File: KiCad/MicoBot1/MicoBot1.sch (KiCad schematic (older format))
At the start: 20 parts, among them J1 Prog, J2 Bat, J3 Motor2, J4 Motor1, J5 Datos, J6 Vcc, J7 Gnd, SW1 Rst, SW2 On, U1 ATmega328P-PU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

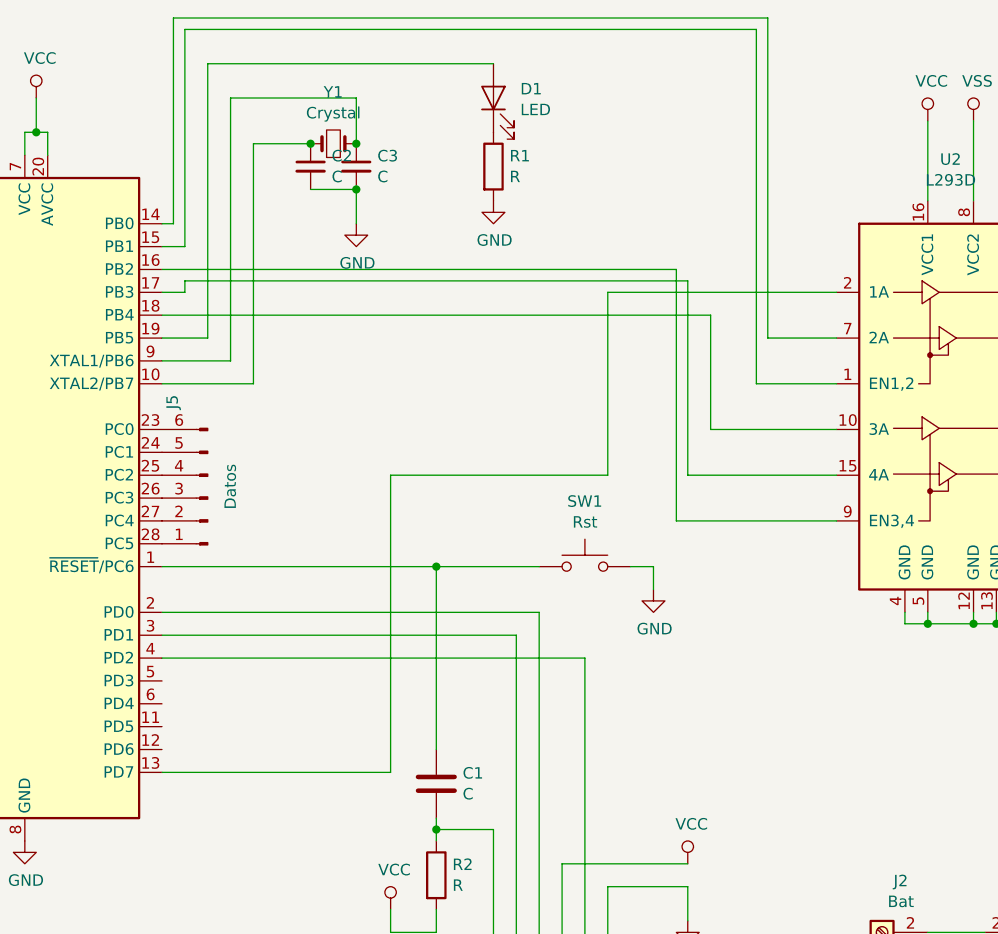
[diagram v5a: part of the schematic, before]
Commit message: 
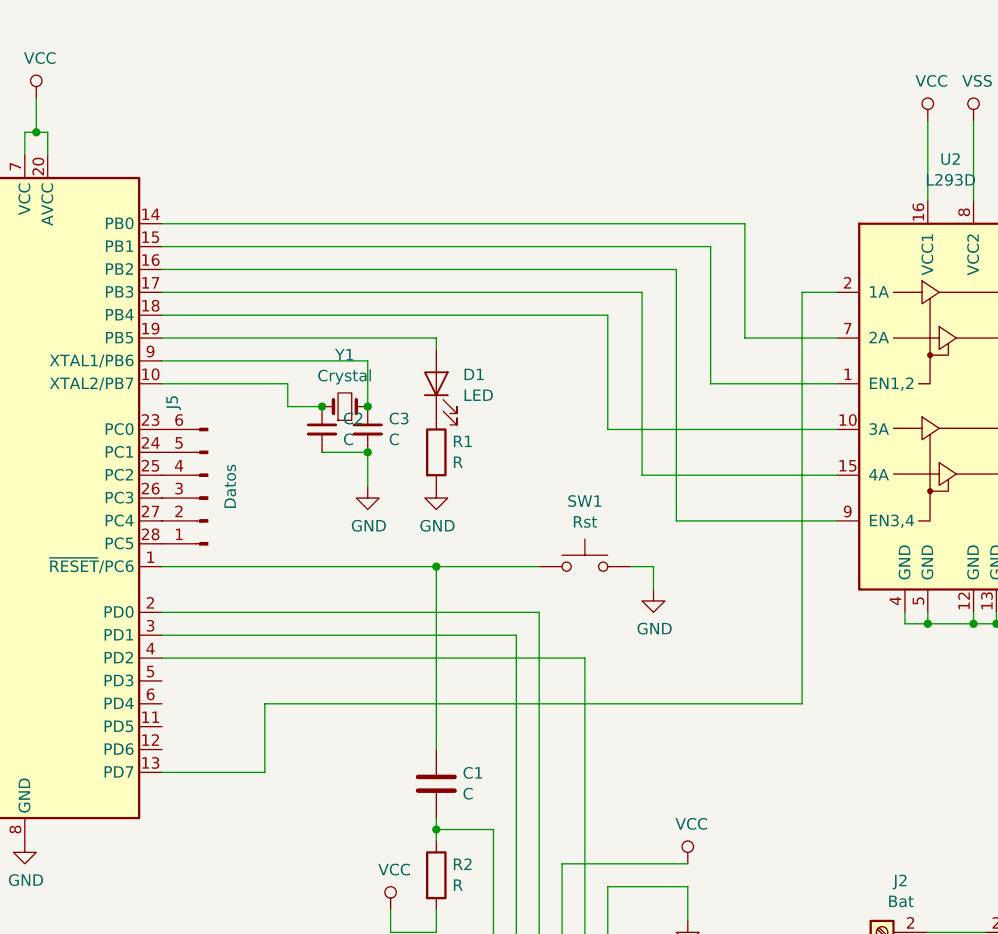
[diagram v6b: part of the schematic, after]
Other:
- moved on the sheet: C2, C3, D1, R1, Y1
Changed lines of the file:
@@
 L Device:LED D1
 U 1 1 5CB896AF
-P 5600 1200
-F 0 "D1" V 5639 1083 50  0000 R CNN
-F 1 "LED" V 5548 1083 50  0000 R CNN
-F 2 "LED_THT:LED_D3.0mm" H 5600 1200 50  0001 C CNN
-F 3 "~" H 5600 1200 50  0001 C CNN
-	1    5600 1200
+P 5350 2450
+F 0 "D1" V 5389 2333 50  0000 R CNN
+F 1 "LED" V 5298 2333 50  0000 R CNN
+F 2 "LED_THT:LED_D3.0mm" H 5350 2450 50  0001 C CNN
+F 3 "~" H 5350 2450 50  0001 C CNN
+	1    5350 2450
 	0    -1   -1   0
 $EndComp
@@
 L Device:R R1
 U 1 1 5CB8BF62
-P 5600 1500
-F 0 "R1" H 5670 1546 50  0000 L CNN
-F 1 "R" H 5670 1455 50  0000 L CNN
-F 2 "Resistor_THT:R_Axial_DIN0204_L3.6mm_D1.6mm_P5.08mm_Horizontal" V 5530 1500 50  0001 C CNN
-F 3 "~" H 5600 1500 50  0001 C CNN
-	1    5600 1500
+P 5350 2750
+F 0 "R1" H 5420 2796 50  0000 L CNN
+F 1 "R" H 5420 2705 50  0000 L CNN
+F 2 "Resistor_THT:R_Axial_DIN0204_L3.6mm_D1.6mm_P5.08mm_Horizontal" V 5280 2750 50  0001 C CNN
+F 3 "~" H 5350 2750 50  0001 C CNN
+	1    5350 2750
 	1    0    0    -1
 $EndComp
@@
 L power:GND #PWR06
 U 1 1 5CB8C74D
-P 5600 1650
-F 0 "#PWR06" H 5600 1400 50  0001 C CNN
-F 1 "GND" H 5605 1477 50  0000 C CNN
-F 2 "" H 5600 1650 50  0001 C CNN
-F 3 "" H 5600 1650 50  0001 C CNN
-	1    5600 1650
+P 5350 2900
+F 0 "#PWR06" H 5350 2650 50  0001 C CNN
+F 1 "GND" H 5355 2727 50  0000 C CNN
+F 2 "" H 5350 2900 50  0001 C CNN
+F 3 "" H 5350 2900 50  0001 C CNN
+	1    5350 2900
 	1    0    0    -1
 $EndComp
@@
 L Device:Crystal_Small Y1
 U 1 1 5CB975FD
-P 4900 1400
-F 0 "Y1" H 4900 1625 50  0000 C CNN
-F 1 "Crystal" H 4900 1534 50  0000 C CNN
-F 2 "Crystal:Crystal_HC49-4H_Vertical" H 4900 1400 50  0001 C CNN
-F 3 "~" H 4900 1400 50  0001 C CNN
-	1    4900 1400
+P 4950 2550
+F 0 "Y1" H 4950 2775 50  0000 C CNN
+F 1 "Crystal" H 4950 2684 50  0000 C CNN
+F 2 "Crystal:Crystal_HC49-4H_Vertical" H 4950 2550 50  0001 C CNN
+F 3 "~" H 4950 2550 50  0001 C CNN
+	1    4950 2550
 	1    0    0    -1
 $EndComp
@@
 L Device:C_Small C2
 U 1 1 5CB99E74
-P 4800 1500
-F 0 "C2" H 4892 1546 50  0000 L CNN
-F 1 "C" H 4892 1455 50  0000 L CNN
-F 2 "Capacitor_THT:C_Disc_D4.3mm_W1.9mm_P5.00mm" H 4800 1500 50  0001 C CNN
-F 3 "~" H 4800 1500 50  0001 C CNN
-	1    4800 1500
+P 4850 2650
+F 0 "C2" H 4942 2696 50  0000 L CNN
+F 1 "C" H 4942 2605 50  0000 L CNN
+F 2 "Capacitor_THT:C_Disc_D4.3mm_W1.9mm_P5.00mm" H 4850 2650 50  0001 C CNN
+F 3 "~" H 4850 2650 50  0001 C CNN
+	1    4850 2650
 	1    0    0    -1
 $EndComp
@@
 L Device:C_Small C3
 U 1 1 5CB9B3E9
-P 5000 1500
-F 0 "C3" H 5092 1546 50  0000 L CNN
-F 1 "C" H 5092 1455 50  0000 L CNN
-F 2 "Capacitor_THT:C_Disc_D4.3mm_W1.9mm_P5.00mm" H 5000 1500 50  0001 C CNN
-F 3 "~" H 5000 1500 50  0001 C CNN
-	1    5000 1500
+P 5050 2650
+F 0 "C3" H 5142 2696 50  0000 L CNN
+F 1 "C" H 5142 2605 50  0000 L CNN
+F 2 "Capacitor_THT:C_Disc_D4.3mm_W1.9mm_P5.00mm" H 5050 2650 50  0001 C CNN
+F 3 "~" H 5050 2650 50  0001 C CNN
+	1    5050 2650
 	1    0    0    -1
 $EndComp
@@
 L power:GND #PWR07
 U 1 1 5CB9B8B0
-P 5000 1750
-F 0 "#PWR07" H 5000 1500 50  0001 C CNN
-F 1 "GND" H 5005 1577 50  0000 C CNN
-F 2 "" H 5000 1750 50  0001 C CNN
-F 3 "" H 5000 1750 50  0001 C CNN
-	1    5000 1750
-	1    0    0    -1
-$EndComp
-Wire Wire Line
-	4800 1600 5000 1600
-Wire Wire Line
-	5000 1750 5000 1600
-Connection ~ 5000 1600
+P 5050 2900
+F 0 "#PWR07" H 5050 2650 50  0001 C CNN
+F 1 "GND" H 5055 2727 50  0000 C CNN
+F 2 "" H 5050 2900 50  0001 C CNN
+F 3 "" H 5050 2900 50  0001 C CNN
+	1    5050 2900
+	1    0    0    -1
+$EndComp
+Wire Wire Line
+	4850 2750 5050 2750
+Wire Wire Line
+	5050 2900 5050 2750
+Connection ~ 5050 2750
 $Comp
 L power:GND #PWR08
@@
 $EndComp
 Wire Wire Line
-	4150 2250 4350 2250
-Wire Wire Line
-	4350 1050 5600 1050
-Wire Wire Line
-	4150 2350 4450 2350
-Wire Wire Line
-	4450 1200 5000 1200
-Wire Wire Line
-	5000 1200 5000 1400
-Connection ~ 5000 1400
-Wire Wire Line
-	4550 1400 4800 1400
-Wire Wire Line
-	4150 2450 4550 2450
-Connection ~ 4800 1400
+	5050 2350 5050 2550
+Connection ~ 5050 2550
+Connection ~ 4850 2550
 $Comp
 L Connector:Screw_Terminal_01x02 J3
@@
 	8250 4950 8300 4950
 Wire Wire Line
-	4150 4150 5150 4150
-Wire Wire Line
-	5150 2850 6100 2850
-Wire Wire Line
-	4150 1750 4200 1750
-Wire Wire Line
-	4200 1750 4200 850
-Wire Wire Line
-	4200 850  6800 850
-Wire Wire Line
-	6800 850  6800 2250
-Wire Wire Line
-	6800 2250 7100 2250
-Wire Wire Line
-	4150 1850 4250 1850
-Wire Wire Line
-	4250 1850 4250 900
-Wire Wire Line
-	4250 900  6750 900
-Wire Wire Line
-	6750 900  6750 2450
-Wire Wire Line
-	6750 2450 7100 2450
-Wire Wire Line
-	6550 2650 7100 2650
-Wire Wire Line
-	6450 2850 7100 2850
-Wire Wire Line
 	6400 3050 7100 3050
-Wire Wire Line
-	6100 2050 6100 2850
-Wire Wire Line
-	5150 2850 5150 4150
-Wire Wire Line
-	4550 1400 4550 2450
-Wire Wire Line
-	4450 1200 4450 2350
-Wire Wire Line
-	4350 1050 4350 2250
-Wire Wire Line
-	6100 2050 7100 2050
-Wire Wire Line
-	6450 2000 4250 2000
-Wire Wire Line
-	4250 2000 4250 2050
-Wire Wire Line
-	4250 2050 4150 2050
-Wire Wire Line
-	6450 2000 6450 2850
 Wire Wire Line
 	4150 1950 6400 1950
@@
 	5350 4850 5350 4750
 Wire Wire Line
-	4150 2150 6550 2150
-Wire Wire Line
-	6550 2150 6550 2650
-Wire Wire Line
 	8600 5250 8600 5350
 $Comp
@@
 Wire Wire Line
 	6000 3650 6000 4950
+Wire Wire Line
+	4150 4150 4600 4150
+Wire Wire Line
+	4600 4150 4600 3850
+Wire Wire Line
+	4600 3850 6950 3850
+Wire Wire Line
+	6950 3850 6950 2050
+Wire Wire Line
+	6950 2050 7100 2050
+Wire Wire Line
+	4150 2150 6100 2150
+Wire Wire Line
+	4150 2050 6250 2050
+Wire Wire Line
+	4700 2550 4850 2550
+Wire Wire Line
+	4150 2350 5050 2350
+Wire Wire Line
+	4700 2450 4700 2550
+Wire Wire Line
+	4150 2450 4700 2450
+Wire Wire Line
+	5350 2300 5350 2250
+Wire Wire Line
+	4150 2250 5350 2250
+Wire Wire Line
+	6100 2650 6100 2150
+Wire Wire Line
+	6100 2650 7100 2650
+Wire Wire Line
+	6250 2850 6250 2050
+Wire Wire Line
+	6250 2850 7100 2850
+Wire Wire Line
+	6550 1850 6550 2450
+Wire Wire Line
+	4150 1850 6550 1850
+Wire Wire Line
+	6550 2450 7100 2450
+Wire Wire Line
+	6700 1750 6700 2250
+Wire Wire Line
+	4150 1750 6700 1750
+Wire Wire Line
+	6700 2250 7100 2250
 $EndSCHEMATC

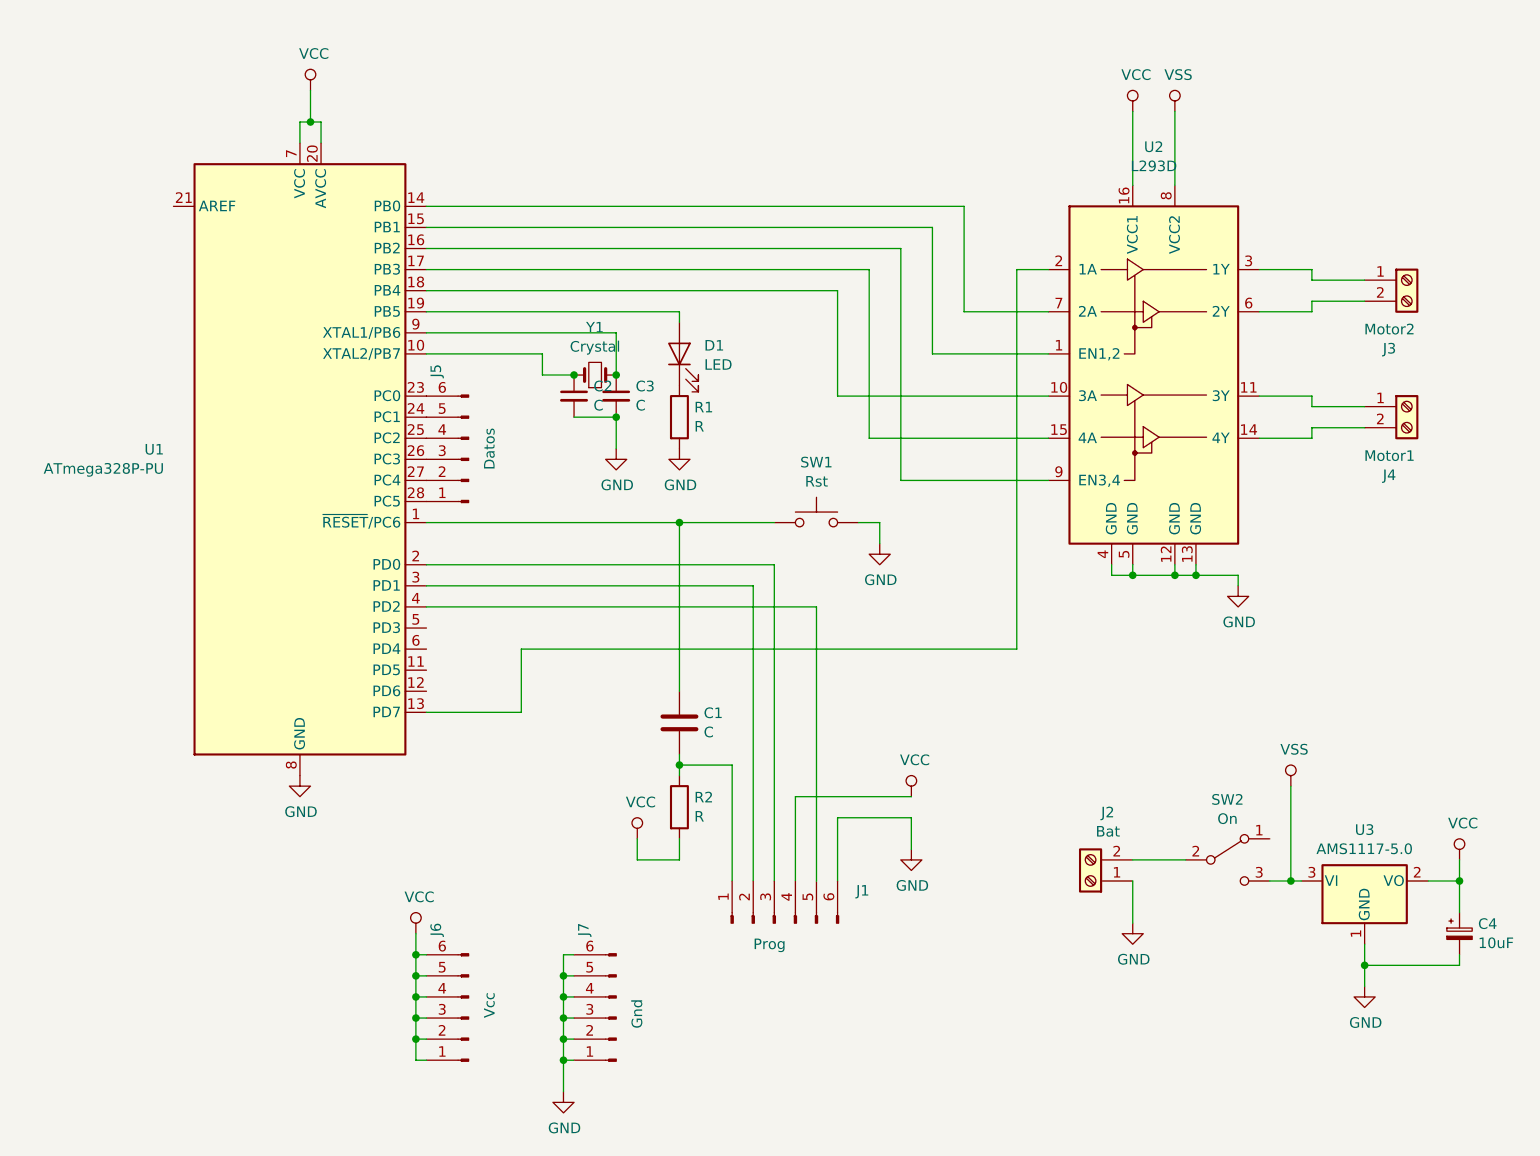
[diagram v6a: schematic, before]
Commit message: 
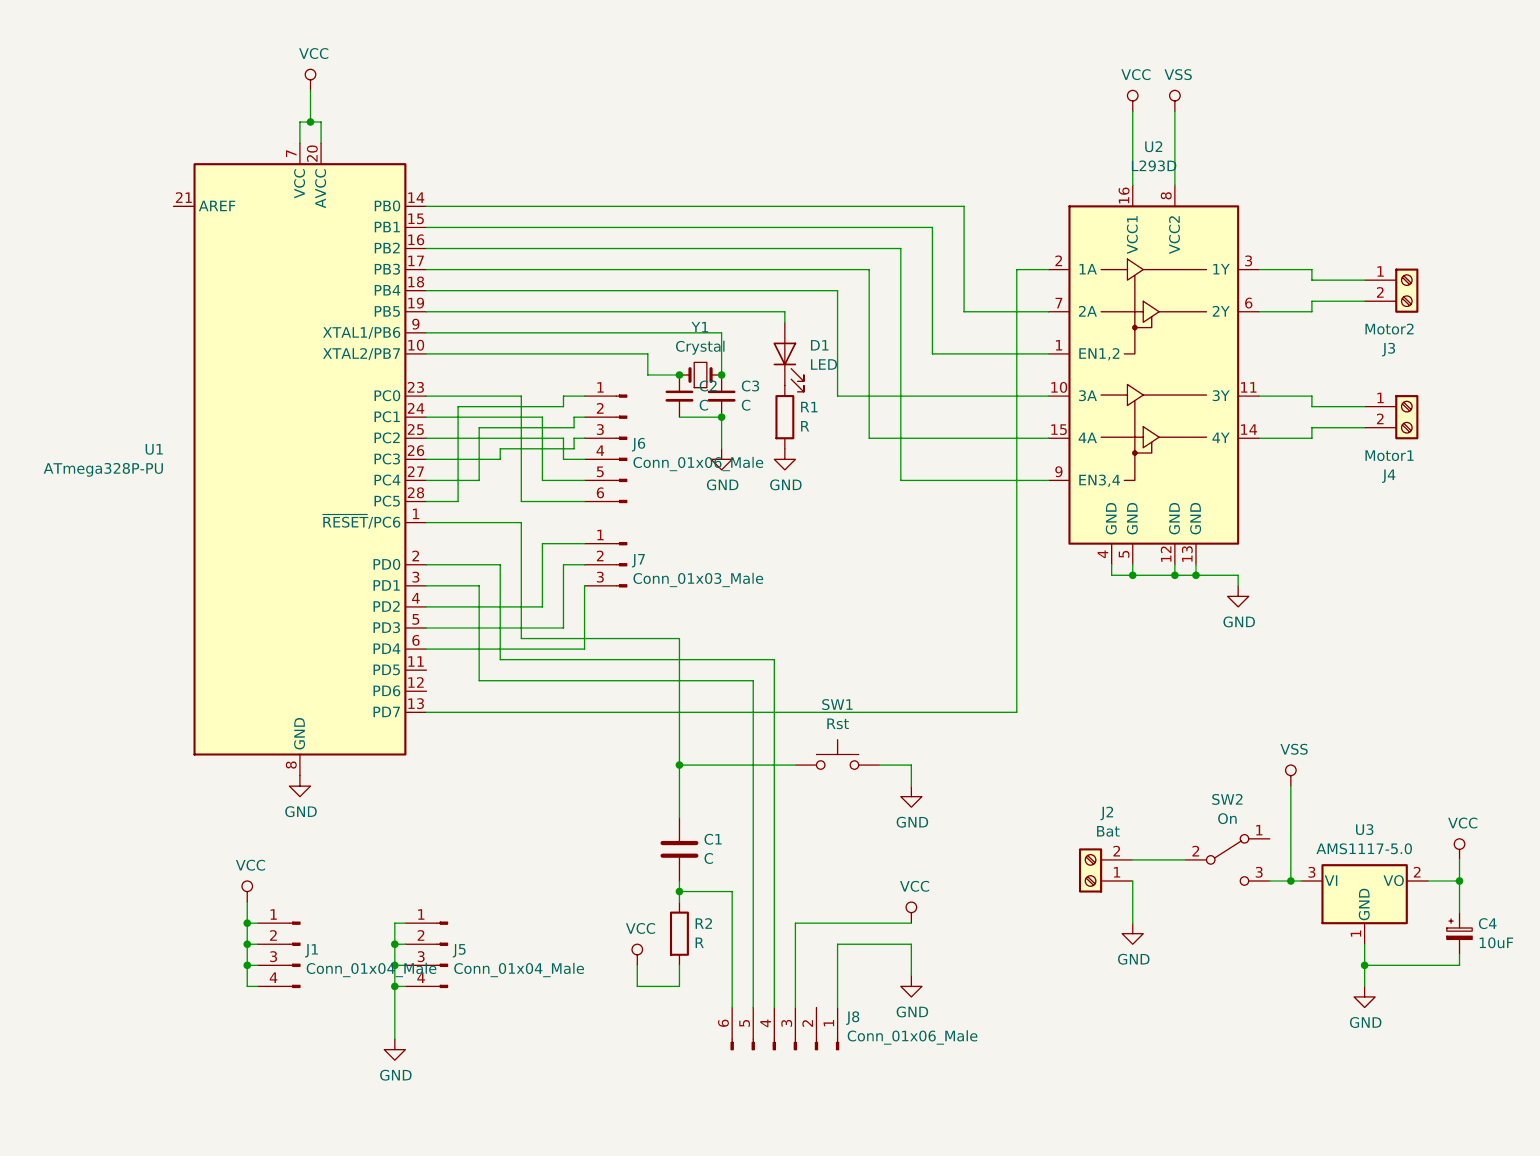
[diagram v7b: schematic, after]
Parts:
- removed J1: Prog, Connector_PinHeader_2.54mm:PinHeader_1x06_P2.54mm_Vertical, symbol Connector:Conn_01x06_Male
- removed J5: Datos, Connector_PinHeader_2.54mm:PinHeader_1x06_P2.54mm_Vertical, symbol Connector:Conn_01x06_Male
- removed J7: Gnd, Connector_PinHeader_2.54mm:PinHeader_1x06_P2.54mm_Vertical, symbol Connector:Conn_01x06_Male
- added J1, J5: Conn_01x04_Male, Connector_PinHeader_2.54mm:PinHeader_1x04_P2.54mm_Vertical, symbol Connector:Conn_01x04_Male
- added J7: Conn_01x03_Male, Connector_PinHeader_2.54mm:PinHeader_1x03_P2.54mm_Vertical, symbol Connector:Conn_01x03_Male
- added J8: Conn_01x06_Male, Connector_PinHeader_2.54mm:PinHeader_1x06_P2.54mm_Vertical, symbol Connector:Conn_01x06_Male
- J6: value Vcc -> Conn_01x06_Male
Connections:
- net GND: now also J5.1 (Pin_1), J5.2 (Pin_2), J5.3 (Pin_3), J5.4 (Pin_4), J8.1 (Pin_1)
- net VCC: now also J1.1 (Pin_1), J1.2 (Pin_2), J1.3 (Pin_3), J1.4 (Pin_4), J8.3 (Pin_3); no longer J6.1 (Pin_1), J6.2 (Pin_2), J6.3 (Pin_3), J6.4 (Pin_4), J6.5 (Pin_5), J6.6 (Pin_6)
- net at U1.2 (PD0): now also J8.4 (Pin_4)
- net at U1.23 (PC0): now also J6.6 (Pin_6)
- net at U1.24 (PC1): now also J6.5 (Pin_5)
- net at U1.25 (PC2): now also J6.4 (Pin_4)
- net at U1.26 (PC3): now also J6.3 (Pin_3)
- net at U1.27 (PC4): now also J6.2 (Pin_2)
- net at U1.28 (PC5): now also J6.1 (Pin_1)
- net at U1.3 (PD1): now also J8.5 (Pin_5)
- net at U1.4 (PD2): now also J7.1 (Pin_1)
- net at U1.5 (PD3): now also J7.2 (Pin_2)
- net at U1.6 (PD4): now also J7.3 (Pin_3)
- net at C1.2, R2.1: now also J8.6 (Pin_6)
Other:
- moved on the sheet: C1, C2, C3, D1, R1, R2, SW1, Y1
